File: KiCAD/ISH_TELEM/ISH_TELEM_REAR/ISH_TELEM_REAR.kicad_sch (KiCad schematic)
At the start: 18 parts, among them Q1 2N7000, U1 MCP3424, U2 MCP1703Ax-400xxTT

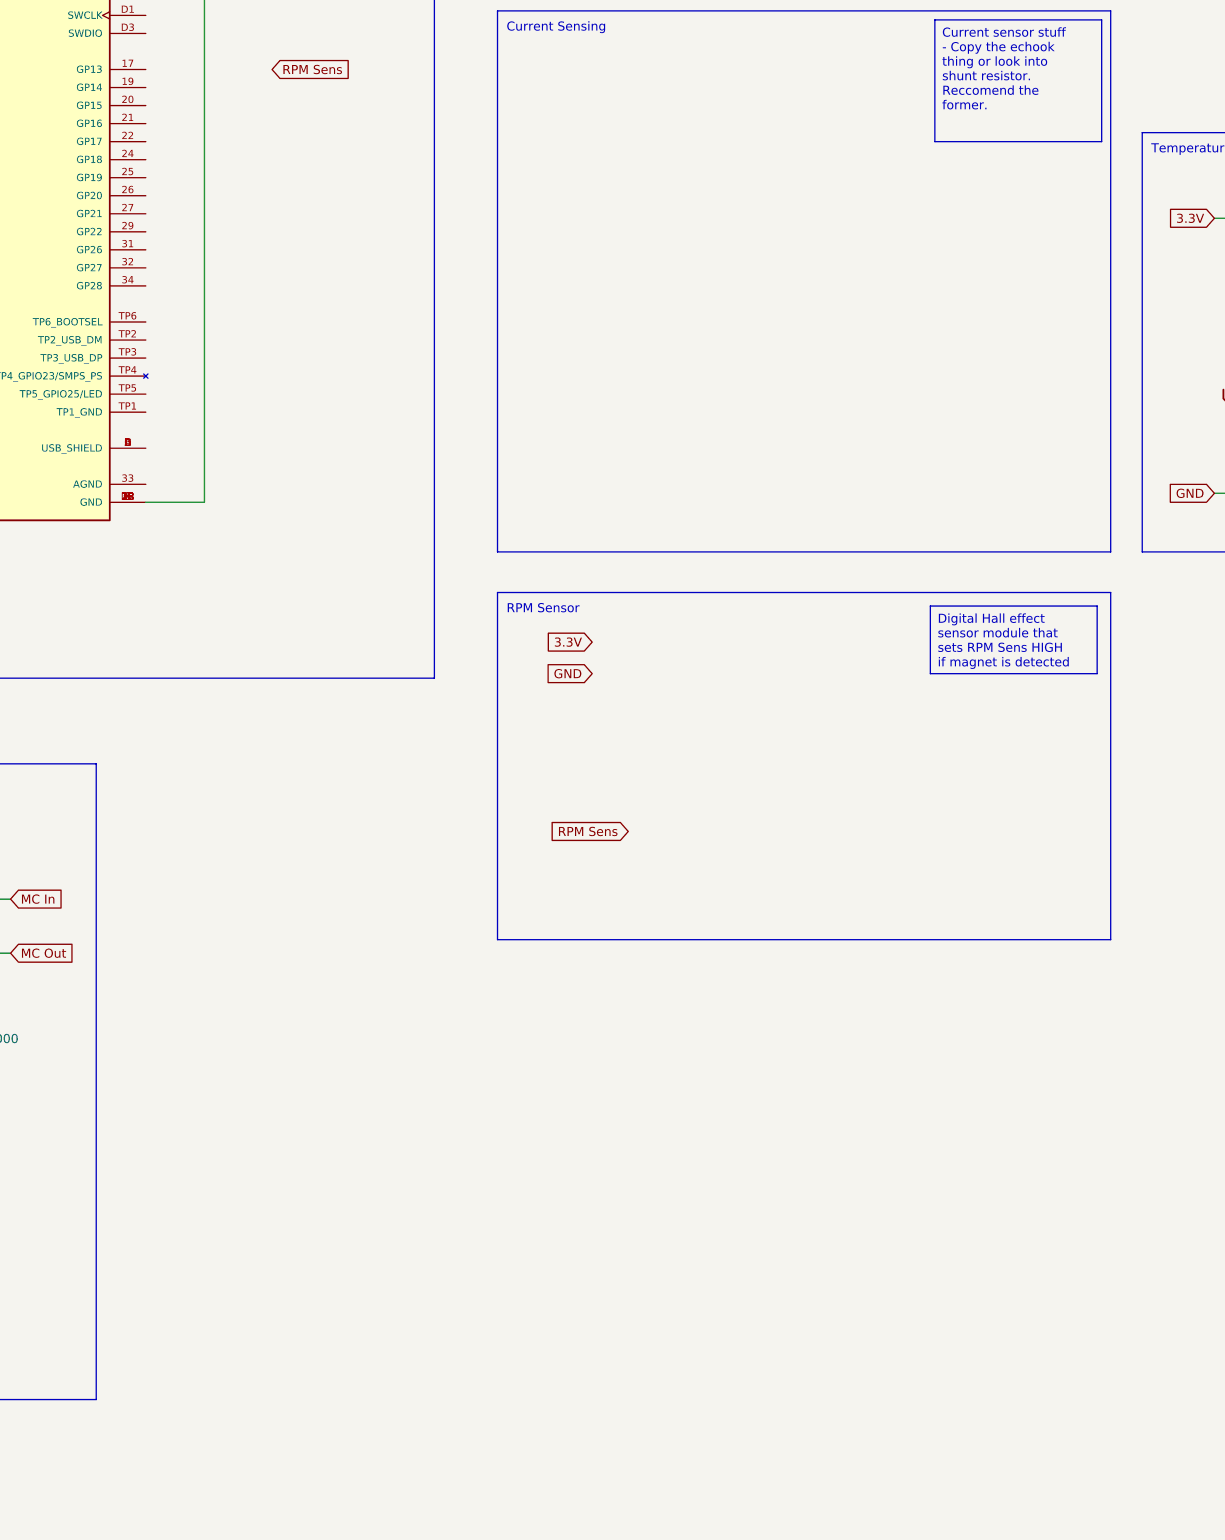
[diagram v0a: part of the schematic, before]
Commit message: Added schematic for the front pcb thing
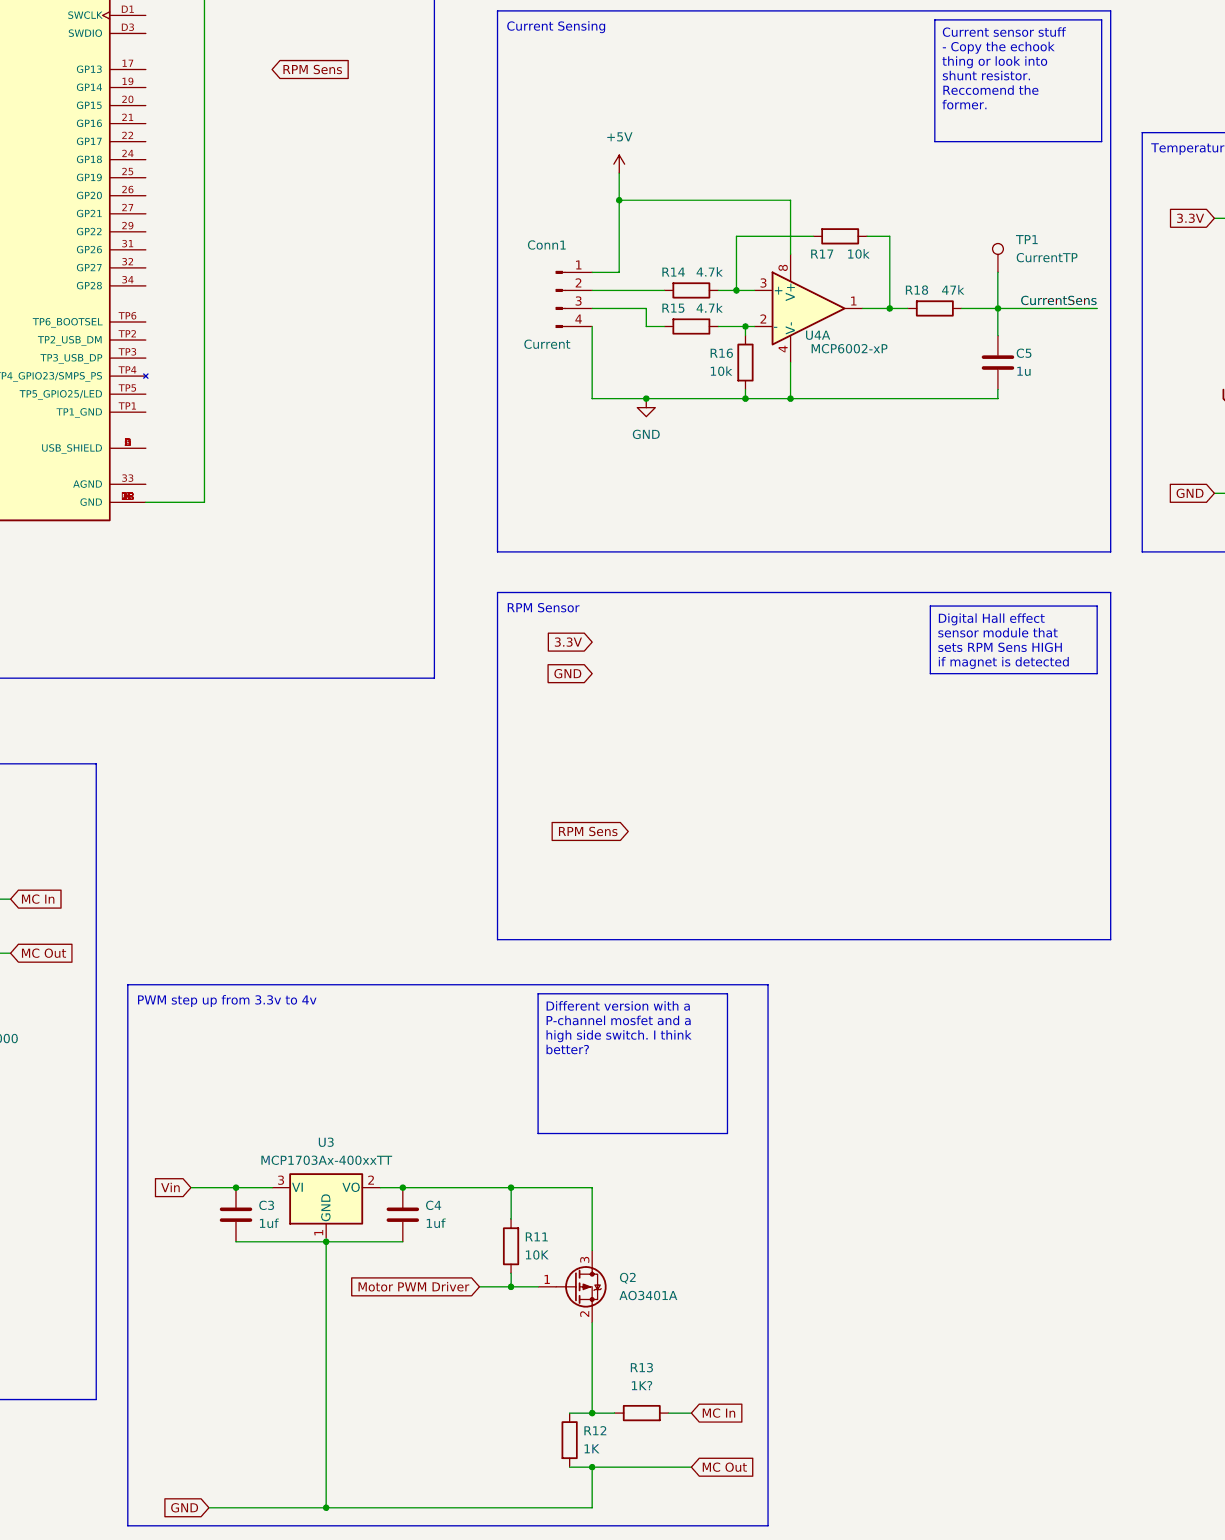
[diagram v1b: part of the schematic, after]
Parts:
- added C3, C4: 1uf, symbol Device:C
- added C5: 1u, Capacitor_THT:C_Disc_D5.1mm_W3.2mm_P5.00mm, symbol Device:C
- added Conn1: Current, user:Pluggable_Terminal_4_5.08mm, symbol Connector:Conn_01x04_Male
- added Q2: AO3401A, Package_TO_SOT_SMD:SOT-23, symbol Transistor_FET:AO3401A
- added R11: 10K, symbol Device:R
- added R12: 1K, symbol Device:R
- added R13: 1K?, symbol Device:R
- added R14, R15: 4.7k, Resistor_THT:R_Axial_DIN0207_L6.3mm_D2.5mm_P10.16mm_Horizontal, symbol Device:R
- added R16, R17: 10k, Resistor_THT:R_Axial_DIN0207_L6.3mm_D2.5mm_P10.16mm_Horizontal, symbol Device:R
- added R18: 47k, Resistor_THT:R_Axial_DIN0207_L6.3mm_D2.5mm_P10.16mm_Horizontal, symbol Device:R
- added TP1: CurrentTP, TestPoint:TestPoint_Pad_D3.0mm, symbol Connector:TestPoint
- added U3: MCP1703Ax-400xxTT, Package_TO_SOT_SMD:SOT-23, symbol Regulator_Linear:MCP1703Ax-400xxTT
- added U4: MCP6002-xP, Package_DIP:DIP-8_W7.62mm_LongPads, symbol Amplifier_Operational:MCP6002-xP
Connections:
- net MC Out is gone; now on net GND: Q1.3 (D), R10.2
- net GND: now also C3.2, C4.2, C5.2, Conn1.4 (Pin_4), R12.2, R16.2, U3.1 (GND), U4.4 (V-)
- net MC In: now also R13.2
- net Motor PWM Driver: now also Q2.1 (G), R11.1
- net Vin: now also C3.1, U3.3 (VI)
- new net: R17.1, R18.2, U4.1
- new net: R14.1, R17.2, U4.3 (+)
- new net: Q2.2 (S), R12.1, R13.1
- new net: C4.1, Q2.3 (D), R11.2, U3.2 (VO)
- new net: Conn1.2 (Pin_2), R14.2
- new net: Conn1.3 (Pin_3), R15.2
- new net: R15.1, R16.1, U4.2 (-)
- new net +5V: Conn1.1 (Pin_1), U4.8 (V+)
- new net CurrentSens: C5.1, R18.1, TP1.1

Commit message: Changed some stuff for the ADC
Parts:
- removed U1: MCP3424, symbol Analog_ADC:MCP3424
- added U1, U5: ADS1115IDGS, Package_SO:TSSOP-10_3x3mm_P0.5mm, symbol Analog_ADC:ADS1115IDGS
- R10: value 1K -> 10K
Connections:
- net GND: now also U1.1 (ADDR), U1.3 (GND), U5.3 (GND)
- net Motor Controller Temp: now also U1.7 (AIN3)
- net Motor Temp: now also U1.6 (AIN2)
- net Reduced Bat1V: now also U1.5 (AIN1)
- net Reduced TotalV: now also U1.4 (AIN0)
- net Vin: no longer MC.39 (VSYS)
- new net Current: U5.4 (AIN0)
- new net Vin (9V): MC.39 (VSYS), U1.8 (VDD), U5.1 (ADDR), U5.8 (VDD)
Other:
- note added: "Current Sensing (Need to look into this)"
- note removed: "Current Sensing"
- moved on the sheet: R5, R6, R7, R8, TH1, TH2

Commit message: Started understanding the current sens stuff, and made a few adjustments
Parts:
- removed TP1: CurrentTP, TestPoint:TestPoint_Pad_D3.0mm, symbol Connector:TestPoint
- added C6, C7: 1uf, symbol Device:C
- added D1: D_Schottky, symbol Device:D_Schottky
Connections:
- net CurrentSens is gone; now on net Current: C5.1, R18.1
- net GND: now also C6.2, C7.2
- net MC In: now also C7.1
- net Vin: now also C6.1
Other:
- note added: "Might actually be best to go for an esp32, least confusion for people used to arduinos"
- note added: "Or diode here. Not really sure about this section, best to just experiment when we work on a breadboard I think."
- note added: "PWM step up from 3.3v to 4v (Alternative)"
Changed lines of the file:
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@@
   (junction (at 78.74 230.505) (diameter 0) (color 0 0 0 0)
   )
+  (junction (at 47.625 193.04) (diameter 0) (color 0 0 0 0)
+  )
   (junction (at 221.615 108.585) (diameter 0) (color 0 0 0 0)
   )
@@
   (junction (at 200.025 106.045) (diameter 0) (color 0 0 0 0)
   )
+  (junction (at 57.785 185.42) (diameter 0) (color 0 0 0 0)
+  )
+  (junction (at 34.29 185.42) (diameter 0) (color 0 0 0 0)
+  )
   (junction (at 187.96 50.165) (diameter 0) (color 0 0 0 0)
   )
@@
     (stroke (width 0) (type default))
   )
-  (wire (pts (xy 236.855 103.505) (xy 236.855 108.585))
-    (stroke (width 0) (type default))
-  )
   (wire (pts (xy 179.705 271.78) (xy 179.705 277.495))
     (stroke (width 0) (type default))
@@
     (stroke (width 0) (type default))
   )
-  (wire (pts (xy 236.855 112.395) (xy 236.855 108.585))
-    (stroke (width 0) (type default))
-  )
   (wire (pts (xy 307.34 97.79) (xy 317.5 97.79))
     (stroke (width 0) (type default))
@@
     (stroke (width 0) (type default))
   )
-  (wire (pts (xy 236.855 108.585) (xy 250.825 108.585))
+  (wire (pts (xy 236.855 108.585) (xy 242.57 108.585))
     (stroke (width 0) (type default))
   )
@@
     (stroke (width 0) (type default))
   )
-  (wire (pts (xy 28.575 185.42) (xy 40.005 185.42))
+  (wire (pts (xy 28.575 185.42) (xy 34.29 185.42))
     (stroke (width 0) (type default))
   )
@@
     (stroke (width 0) (type default))
   )
-  (wire (pts (xy 55.245 185.42) (xy 88.9 185.42))
+  (wire (pts (xy 55.245 185.42) (xy 57.785 185.42))
     (stroke (width 0) (type default))
   )
@@
     (stroke (width 0) (type default))
   )
+  (wire (pts (xy 57.785 185.42) (xy 88.9 185.42))
+    (stroke (width 0) (type default))
+  )
   (wire (pts (xy 234.315 29.21) (xy 234.315 32.385))
     (stroke (width 0) (type default))
@@
     (stroke (width 0) (type default))
   )
+  (wire (pts (xy 34.29 193.04) (xy 47.625 193.04))
+    (stroke (width 0) (type default))
+  )
   (wire (pts (xy 267.335 117.475) (xy 270.51 117.475))
     (stroke (width 0) (type default))
@@
     (stroke (width 0) (type default))
   )
+  (wire (pts (xy 236.855 108.585) (xy 236.855 112.395))
+    (stroke (width 0) (type default))
+  )
   (wire (pts (xy 244.475 42.545) (xy 250.19 42.545))
     (stroke (width 0) (type default))
@@
     (stroke (width 0) (type default))
   )
+  (wire (pts (xy 34.29 185.42) (xy 40.005 185.42))
+    (stroke (width 0) (type default))
+  )
   (wire (pts (xy 187.96 40.005) (xy 187.96 42.545))
     (stroke (width 0) (type default))
@@
     (stroke (width 0) (type default))
   )
+  (wire (pts (xy 47.625 193.04) (xy 57.785 193.04))
+    (stroke (width 0) (type default))
+  )
   (wire (pts (xy 207.645 100.965) (xy 207.645 93.345))
     (stroke (width 0) (type default))
@@
     (effects (font (size 1.27 1.27)) (justify left top))
   )
-  (text_box "Current sensor stuff - Copy the echook thing or look into shunt resistor. Reccomend the former."
-    (at 227.965 67.945 0) (size 23.495 17.145)
+  (text_box "Current sensor stuff - Copy the echook thing or look into shunt resistor. Reccomend the former. \n\nI added a great video to explain this on the research doc. The Echook documentation also does an alright job."
+    (at 217.805 67.945 0) (size 33.655 20.32)
     (stroke (width 0) (type default))
     (fill (type none))
@@
     (effects (font (size 1.27 1.27)) (justify left bottom))
   )
-  (text "PWM step up from 3.3v to 4v" (at 115.57 207.01 0)
+  (text "PWM step up from 3.3v to 4v (Alternative)\n" (at 115.57 207.01 0)
     (effects (font (size 1.27 1.27)) (justify left bottom))
   )
@@
     (effects (font (size 1.27 1.27)) (justify left bottom))
   )
+  (text "Might actually be best to go for an esp32,\nleast confusion for people used to arduinos"
+    (at 69.85 45.72 0)
+    (effects (font (size 1.27 1.27)) (justify left bottom))
+  )
   (text "Battery V Sensors | Voltage Deviders" (at 167.64 18.415 0)
     (effects (font (size 1.27 1.27)) (justify left bottom))
@@
     (effects (font (size 1.27 1.27)) (justify left bottom))
   )
+  (text "Or diode here. Not really sure about \nthis section, best to just experiment\nwhen we work on a breadboard I think."
+    (at 48.26 202.565 0)
+    (effects (font (size 1.27 1.27)) (justify left bottom))
+  )
   (text "Temperature Sensors\n" (at 258.445 69.85 0)
     (effects (font (size 1.27 1.27)) (justify left bottom))
-  )
-  (label "CurrentSens" (at 250.825 108.585 180) (fields_autoplaced)
-    (effects (font (size 1.27 1.27)) (justify right bottom))
   )
   (label "6_AA_Batteries_(~9V)" (at 20.32 27.94 0) (fields_autoplaced)
@@
     (effects (font (size 1.27 1.27)) (justify left))
     (property "Intersheetrefs" "${INTERSHEET_REFS}" (at 107.6694 199.39 0)
+      (effects (font (size 1.27 1.27)) (justify left) hide)
+    )
+  )
+  (global_label "Current" (shape input) (at 242.57 108.585 0) (fields_autoplaced)
+    (effects (font (size 1.27 1.27)) (justify left))
+    (property "Intersheetrefs" "${INTERSHEET_REFS}" (at 252.5099 108.585 0)
       (effects (font (size 1.27 1.27)) (justify left) hide)
     )
@@
     )
   )
-  (symbol (lib_id "Connector:TestPoint") (at 236.855 103.505 0) (unit 1)
-    (in_bom yes) (on_board yes) (dnp no) (fields_autoplaced)
-    (property "Reference" "TP1" (at 239.395 98.9329 0)
-      (effects (font (size 1.27 1.27)) (justify left))
-    )
-    (property "Value" "CurrentTP" (at 239.395 101.4729 0)
-      (effects (font (size 1.27 1.27)) (justify left))
-    )
-    (property "Footprint" "TestPoint:TestPoint_Pad_D3.0mm" (at 241.935 103.505 0)
-      (effects (font (size 1.27 1.27)) hide)
-    )
-    (property "Datasheet" "~" (at 241.935 103.505 0)
-      (effects (font (size 1.27 1.27)) hide)
-    )
-    (pin "1")
-    (instances
-      (project "ISH_TELEM_REAR"
-        (path "/718ab4f4-a987-4eed-955a-ee8875189be5"
-          (reference "TP1") (unit 1)
-        )
-      )
-      (project "eChook_Nano"
-        (path "/9538e4ed-27e6-4c37-b989-9859dc0d49e8"
-          (reference "TP9") (unit 1)
-        )
-      )
-    )
-  )
   (symbol (lib_id "Device:R") (at 168.275 240.665 180) (unit 1)
     (in_bom yes) (on_board yes) (dnp no) (fields_autoplaced)
@@
         )
       )
+    )
+  )
+  (symbol (lib_id "Device:C") (at 34.29 189.23 0) (unit 1)
+    (in_bom yes) (on_board yes) (dnp no) (fields_autoplaced)
+    (property "Reference" "C6" (at 37.465 187.96 0)
+      (effects (font (size 1.27 1.27)) (justify left))
+    )
+    (property "Value" "1uf" (at 37.465 190.5 0)
+      (effects (font (size 1.27 1.27)) (justify left))
+    )
+    (property "Footprint" "" (at 35.2552 193.04 0)
+      (effects (font (size 1.27 1.27)) hide)
+    )
+    (property "Datasheet" "~" (at 34.29 189.23 0)
+      (effects (font (size 1.27 1.27)) hide)
+    )
+    (pin "1")
+    (pin "2")
+    (instances
+      (project "ISH_TELEM_REAR"
+        (path "/718ab4f4-a987-4eed-955a-ee8875189be5"
+          (reference "C6") (unit 1)
+        )
+      )
+    )
+  )
+  (symbol (lib_id "Device:C") (at 57.785 189.23 0) (unit 1)
+    (in_bom yes) (on_board yes) (dnp no) (fields_autoplaced)
+    (property "Reference" "C7" (at 60.96 187.96 0)
+      (effects (font (size 1.27 1.27)) (justify left))
+    )
+    (property "Value" "1uf" (at 60.96 190.5 0)
+      (effects (font (size 1.27 1.27)) (justify left))
+    )
+    (property "Footprint" "" (at 58.7502 193.04 0)
+      (effects (font (size 1.27 1.27)) hide)
+    )
+    (property "Datasheet" "~" (at 57.785 189.23 0)
+      (effects (font (size 1.27 1.27)) hide)
+    )
+    (pin "1")
+    (pin "2")
+    (instances
+      (project "ISH_TELEM_REAR"
+        (path "/718ab4f4-a987-4eed-955a-ee8875189be5"
+          (reference "C7") (unit 1)
+        )
+      )
+    )
+  )
+  (symbol (lib_id "Device:D_Schottky") (at 80.645 191.77 270) (unit 1)
+    (in_bom yes) (on_board yes) (dnp no)
+    (property "Reference" "D1" (at 76.2 191.135 90)
+      (effects (font (size 1.27 1.27)) (justify left))
+    )
+    (property "Value" "D_Schottky" (at 68.58 193.04 90)
+      (effects (font (size 1.27 1.27)) (justify left))
+    )
+    (property "Footprint" "" (at 80.645 191.77 0)
+      (effects (font (size 1.27 1.27)) hide)
+    )
+    (property "Datasheet" "~" (at 80.645 191.77 0)
+      (effects (font (size 1.27 1.27)) hide)
+    )
+    (pin "1")
+    (pin "2")
+    (instances
+      (project "ISH_TELEM_REAR"
+        (path "/718ab4f4-a987-4eed-955a-ee8875189be5"
+          (reference "D1") (unit 1)
+        )
+      )
